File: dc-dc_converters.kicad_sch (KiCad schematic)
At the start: 63 parts, among them J3 JST_SH_1x4_SM04B-SRSS-TB-LF-SN, J4 Molex_Nano-Fit_1x2_105313-220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, U2 SIC477ED-T1-GE3, U3 AP62301WU-7, U4 AP62301WU-7, U7 AP62301Z6-7

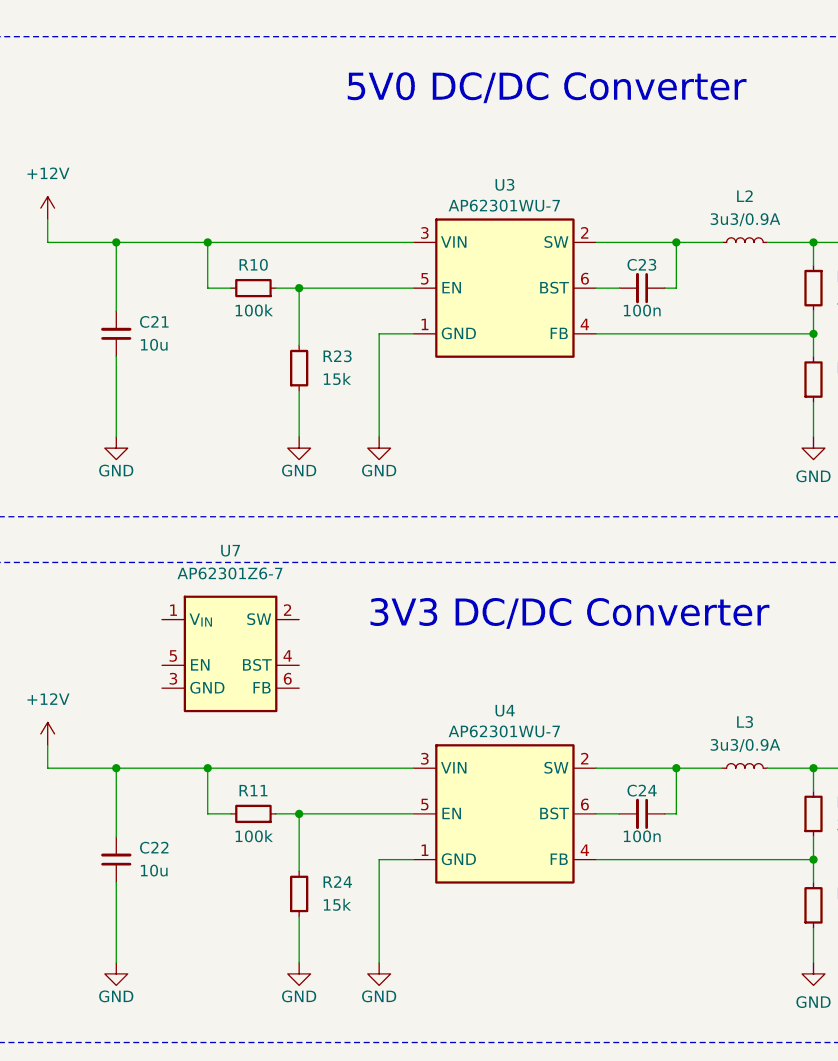
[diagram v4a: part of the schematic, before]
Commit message: [#57006] Change U3 U4 to SOT-563
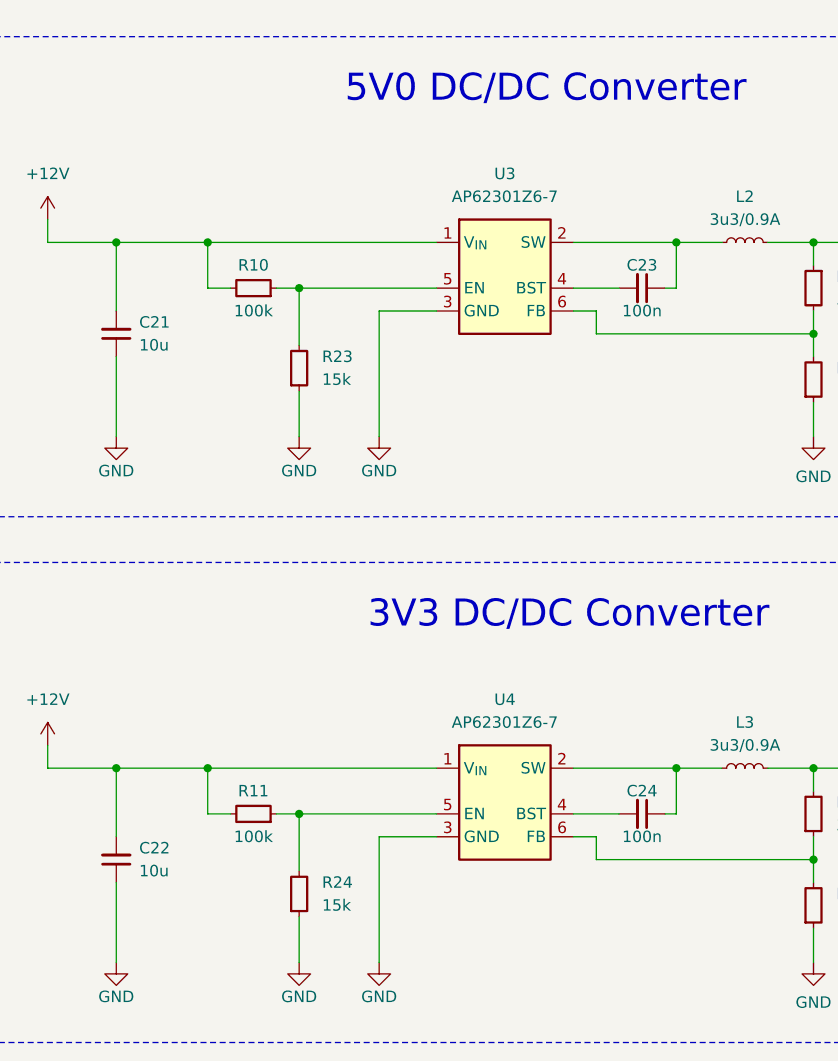
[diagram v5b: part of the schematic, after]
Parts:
- removed U3, U4: AP62301WU-7, antmicro-footprints:TSOT23-6, symbol antmicroDCDCConverters:AP62301_TSOT
- removed U7: AP62301Z6-7, antmicro-footprints:SOT-563, symbol antmicroDCDCConverters:AP62301Z6-7
- added U3, U4: AP62301Z6-7, antmicro-footprints:SOT-563, symbol antmicroDCDCConverters:AP62301Z6-7
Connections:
- net +12V: now also U3.1 (V_{IN}), U4.1 (V_{IN})
- net GND: now also U3.3 (GND), U4.3 (GND)
- net at R10.1, R23.2: now also U3.5 (EN)
- net at C24.1, L3.1: now also U4.2 (SW)
- net at R1.1, R27.2: now also U4.6 (FB)
- net at R11.1, R24.2: now also U4.5 (EN)
- net at C24.2: now also U4.4 (BST)
- net at C23.1, L2.1: now also U3.2 (SW)
- net at C23.2: now also U3.4 (BST)
- net at R2.2, R41.2: now also U3.6 (FB)

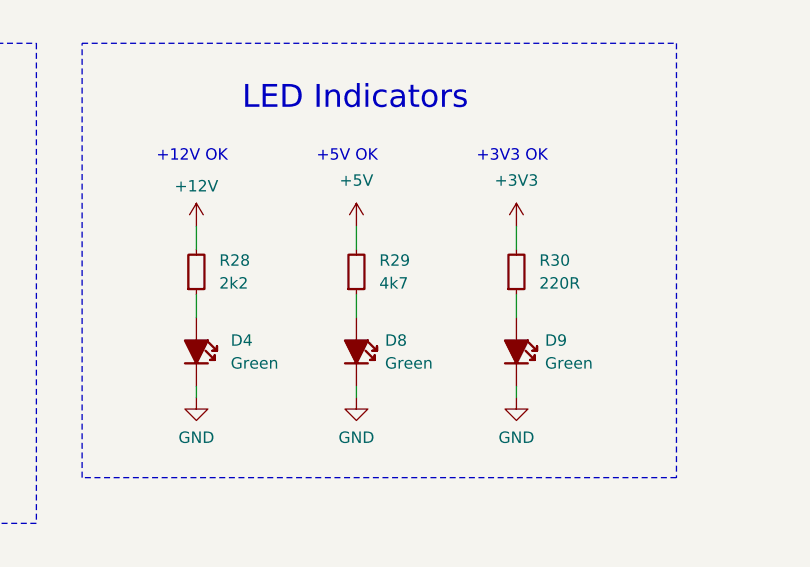
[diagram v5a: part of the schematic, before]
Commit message: [#57006] Fix POWER_OK2, POWER_OK3 LEDs
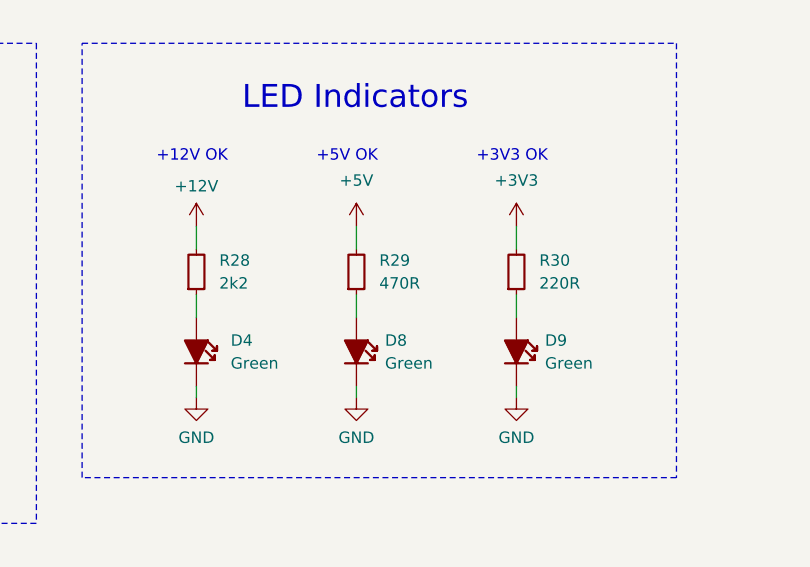
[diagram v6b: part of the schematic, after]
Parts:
- R29: symbol antmicroResistors0402:R_4k7_0402 -> antmicroResistors0402:R_470R_0402; MPN CR0402-FX-4701GLF -> CR0402-FX-4700GLF; Val 4k7 -> 470R
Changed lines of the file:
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@@
     )
   )
-  (symbol (lib_id "antmicroResistors0402:R_4k7_0402") (at 195.58 175.26 90) (unit 1)
+  (symbol (lib_id "antmicroResistors0402:R_470R_0402") (at 195.58 175.26 90) (unit 1)
     (in_bom yes) (on_board yes) (dnp no) (fields_autoplaced)
     (property "Reference" "R29" (at 198.12 171.45 90)
@@
       (effects (font (size 1.27 1.27) (thickness 0.15)) (justify left bottom) hide)
     )
-    (property "MPN" "CR0402-FX-4701GLF" (at 215.9 154.94 0)
+    (property "MPN" "CR0402-FX-4700GLF" (at 215.9 154.94 0)
       (effects (font (size 1.27 1.27) (thickness 0.15)) (justify left bottom) hide)
     )
@@
       (effects (font (size 1.27 1.27) (thickness 0.15)) (justify left bottom) hide)
     )
-    (property "Val" "4k7" (at 198.12 173.99 90)
+    (property "Val" "470R" (at 198.12 173.99 90)
       (effects (font (size 1.27 1.27) (thickness 0.15)) (justify right))
     )

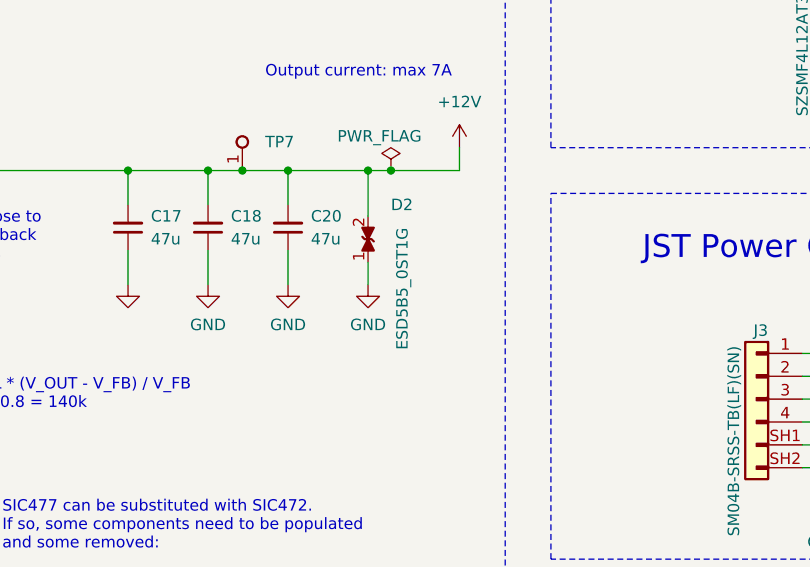
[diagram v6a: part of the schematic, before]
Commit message: [#57006] Change D2 to AXGD10402KR
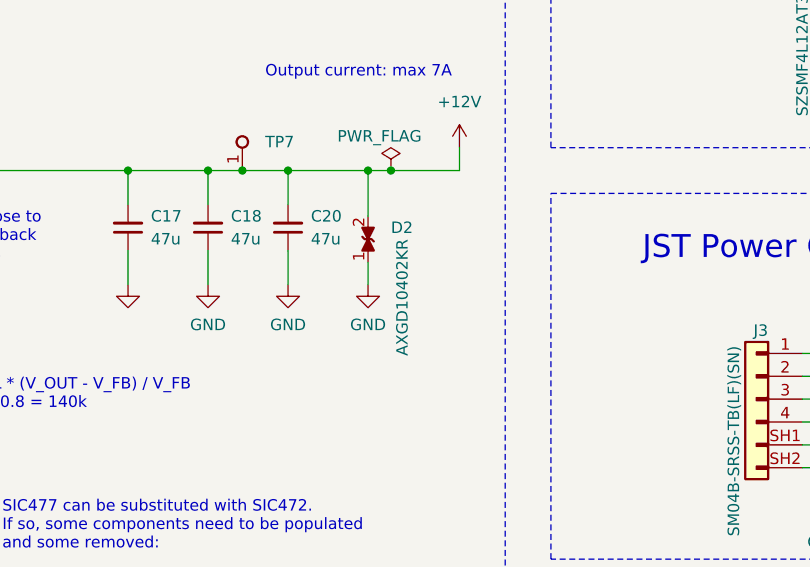
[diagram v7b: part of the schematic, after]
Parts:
- removed D2: ESD5B5_0ST1G, antmicro-footprints:SOD-523_NP, symbol antmicroTVSDiodes:ESD5B5_0ST1G
- added D2: AXGD10402KR, antmicro-footprints:D_0402_1005Metric, symbol antmicroTVSDiodes:AXGD10402KR
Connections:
- net +12V: now also D2.2
- net GND: now also D2.1
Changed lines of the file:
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@@
-    )
-  )
-  (symbol (lib_id "antmicroTVSDiodes:ESD5B5_0ST1G") (at 254 83.82 90) (unit 1)
-    (in_bom yes) (on_board yes) (dnp no)
-    (property "Reference" "D2" (at 256.54 77.4699 90)
-      (effects (font (size 1.27 1.27)) (justify right))
-    )
-    (property "Value" "ESD5B5_0ST1G" (at 257.81 80.01 0)
-      (effects (font (size 1.27 1.27)) (justify right))
-    )
-    (property "Footprint" "antmicro-footprints:SOD-523_NP" (at 248.92 78.74 0)
-      (effects (font (size 1.27 1.27)) (justify left) hide)
-    )
-    (property "Datasheet" "https://www.mouser.com/datasheet/2/308/ESD5B5_0ST1_D-1805066.pdf" (at 246.38 78.74 0)
-      (effects (font (size 1.27 1.27)) (justify left) hide)
-    )
-    (property "Manufacturer" "ON Semiconductor" (at 226.06 78.74 0)
-      (effects (font (size 1.27 1.27)) (justify left) hide)
-    )
-    (property "MPN" "ESD5B5.0ST1G" (at 241.3 78.74 0)
-      (effects (font (size 1.27 1.27)) (justify left) hide)
-    )
-    (property "Author" "Antmicro" (at 274.32 58.42 0)
-      (effects (font (size 1.27 1.27) (thickness 0.15)) (justify left bottom) hide)
-    )
-    (property "License" "Apache-2.0" (at 276.86 58.42 0)
-      (effects (font (size 1.27 1.27) (thickness 0.15)) (justify left bottom) hide)
-    )
-    (pin "1")
-    (pin "2")
-    (instances
-      (project "USB-C-power-adapter"
-        (path "/8da33aa8-79ed-467a-95ed-bf58aa0d1db6/10c37477-f10f-4b8b-8eb5-2eccdd3a4234"
-          (reference "D2") (unit 1)
-        )
-      )
     )
   )
@@
         )
       )
+    )
+  )
+  (symbol (lib_id "antmicroTVSDiodes:AXGD10402KR") (at 254 83.82 90) (unit 1)
+    (in_bom yes) (on_board yes) (dnp no)
+    (property "Reference" "D2" (at 256.54 80.01 90)
+      (effects (font (size 1.27 1.27) (thickness 0.15)) (justify right))
+    )
+    (property "Value" "AXGD10402KR" (at 264.16 58.42 0)
+      (effects (font (size 1.27 1.27) (thickness 0.15)) (justify left bottom) hide)
+    )
+    (property "Footprint" "antmicro-footprints:D_0402_1005Metric" (at 266.7 58.42 0)
+      (effects (font (size 1.27 1.27) (thickness 0.15)) (justify left bottom) hide)
+    )
+    (property "Datasheet" "https://www.littelfuse.com/media?resourcetype=datasheets&itemid=020b2bf2-064c-4ff1-a898-b4ec805b2fea&filename=littelfuse-xtremeguard-axgd-datasheet" (at 269.24 58.42 0)
+      (effects (font (size 1.27 1.27) (thickness 0.15)) (justify left bottom) hide)
+    )
+    (property "Manufacturer" "Littelfuse" (at 271.78 58.42 0)
+      (effects (font (size 1.27 1.27) (thickness 0.15)) (justify left bottom) hide)
+    )
+    (property "MPN" "AXGD10402KR" (at 257.81 81.28 0)
+      (effects (font (size 1.27 1.27) (thickness 0.15)) (justify right))
+    )
+    (property "Author" "Antmicro" (at 274.32 58.42 0)
+      (effects (font (size 1.27 1.27) (thickness 0.15)) (justify left bottom) hide)
+    )
+    (property "License" "Apache-2.0" (at 276.86 58.42 0)
+      (effects (font (size 1.27 1.27) (thickness 0.15)) (justify left bottom) hide)
+    )
+    (pin "2")
+    (pin "1")
+    (instances
+      (project "USB-C-power-adapter"
+        (path "/8da33aa8-79ed-467a-95ed-bf58aa0d1db6/10c37477-f10f-4b8b-8eb5-2eccdd3a4234"
+          (reference "D2") (unit 1)
+        )
+      )

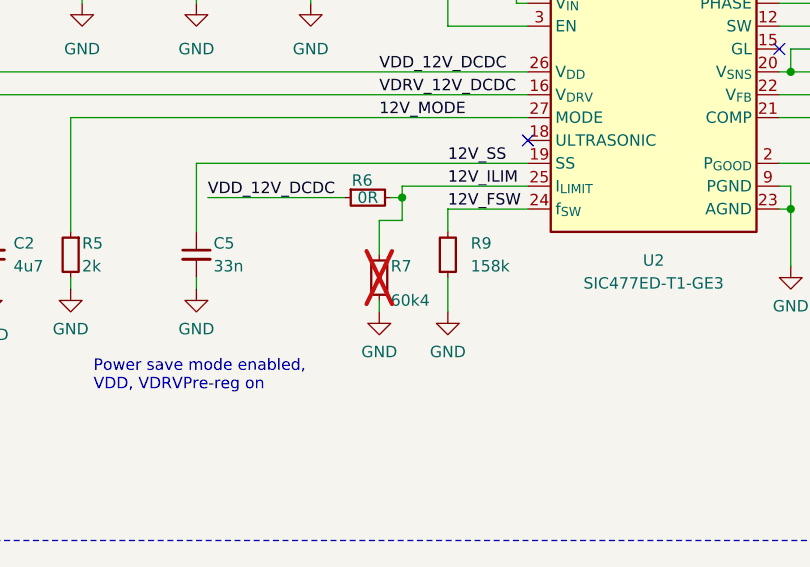
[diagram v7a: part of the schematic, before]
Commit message: [#57006] Change R7 to 68k
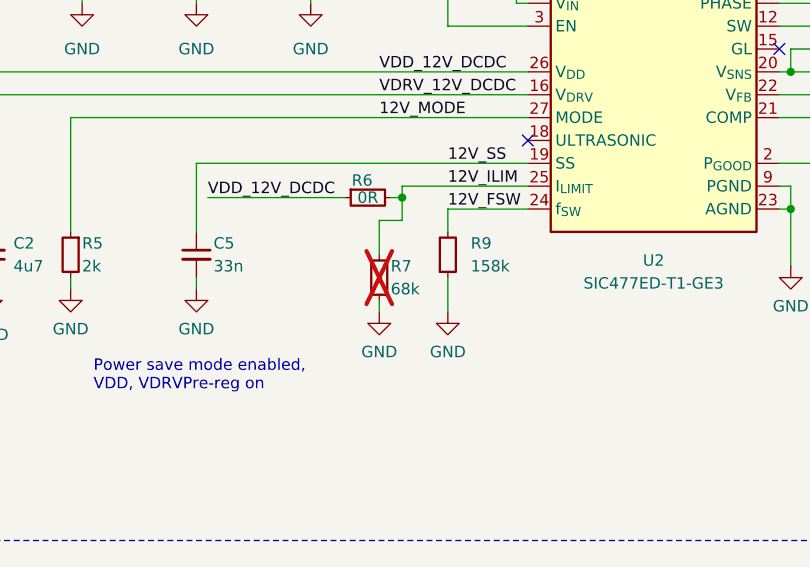
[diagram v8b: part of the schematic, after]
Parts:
- removed R7: R_60k4_0402, antmicro-footprints:R_0402_1005Metric, symbol antmicroResistors0402:R_60k4_0402
- added R7: R_68k_0402, antmicro-footprints:R_0402_1005Metric, symbol antmicroResistors0402:R_68k_0402
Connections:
- net 12V_ILIM: now also R7.2
- net GND: now also R7.1
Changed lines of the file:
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@@
     )
   )
-  (symbol (lib_id "antmicroResistors0402:R_60k4_0402") (at 99.06 110.49 270) (unit 1)
-    (in_bom no) (on_board yes) (dnp yes)
+  (symbol (lib_id "antmicroResistors0402:R_68k_0402") (at 99.06 115.57 90) (unit 1)
+    (in_bom yes) (on_board yes) (dnp yes)
     (property "Reference" "R7" (at 100.33 111.76 90)
-      (effects (font (size 1.27 1.27)) (justify left))
+      (effects (font (size 1.27 1.27) (thickness 0.15)) (justify right))
     )
-    (property "Value" "R_60k4_0402" (at 95.25 110.49 0)
-      (effects (font (size 1.27 1.27)) (justify left) hide)
+    (property "Value" "R_68k_0402" (at 111.76 95.25 0)
+      (effects (font (size 1.27 1.27) (thickness 0.15)) (justify left bottom) hide)
     )
-    (property "Footprint" "antmicro-footprints:R_0402_1005Metric" (at 104.14 115.57 0)
-      (effects (font (size 1.27 1.27)) (justify left) hide)
+    (property "Footprint" "antmicro-footprints:R_0402_1005Metric" (at 114.3 95.25 0)
+      (effects (font (size 1.27 1.27) (thickness 0.15)) (justify left bottom) hide)
     )
-    (property "Datasheet" "https://www.bourns.com/docs/product-datasheets/cr.pdf" (at 99.06 110.49 0)
-      (effects (font (size 1.27 1.27)) (justify left) hide)
+    (property "Datasheet" "https://www.bourns.com/docs/product-datasheets/cr.pdf" (at 116.84 95.25 0)
+      (effects (font (size 1.27 1.27) (thickness 0.15)) (justify left bottom) hide)
     )
-    (property "Manufacturer" "Bourns" (at 109.22 115.57 0)
-      (effects (font (size 1.27 1.27)) (justify left) hide)
+    (property "MPN" "CR0402-FX-6802GLF" (at 119.38 95.25 0)
+      (effects (font (size 1.27 1.27) (thickness 0.15)) (justify left bottom) hide)
     )
-    (property "MPN" "CR0402-FX-6042GLF" (at 106.68 115.57 0)
-      (effects (font (size 1.27 1.27)) (justify left) hide)
+    (property "Manufacturer" "Bourns" (at 121.92 95.25 0)
+      (effects (font (size 1.27 1.27) (thickness 0.15)) (justify left bottom) hide)
     )
-    (property "Val" "60k4" (at 100.33 115.57 90)
-      (effects (font (size 1.27 1.27)) (justify left))
+    (property "License" "Apache-2.0" (at 124.46 95.25 0)
+      (effects (font (size 1.27 1.27) (thickness 0.15)) (justify left bottom) hide)
     )
-    (property "DNP" "DNP" (at 99.06 111.125 0)
-      (effects (font (size 1.27 1.27)) (justify left) hide)
+    (property "Author" "Antmicro" (at 127 95.25 0)
+      (effects (font (size 1.27 1.27) (thickness 0.15)) (justify left bottom) hide)
     )
-    (property "License" "Apache-2.0" (at 73.66 130.81 0)
-      (effects (font (size 1.27 1.27) (thickness 0.15)) (justify left) hide)
+    (property "Val" "68k" (at 100.33 114.3 90)
+      (effects (font (size 1.27 1.27) (thickness 0.15)) (justify right))
     )
-    (property "Author" "Antmicro" (at 71.12 130.81 0)
-      (effects (font (size 1.27 1.27) (thickness 0.15)) (justify left) hide)
-    )
-    (property "Tolerance" "1%" (at 88.9 130.81 0)
-      (effects (font (size 1.27 1.27)) (justify left) hide)
+    (property "Tolerance" "1%" (at 109.22 95.25 0)
+      (effects (font (size 1.27 1.27)) (justify left bottom) hide)
     )
     (pin "1")
